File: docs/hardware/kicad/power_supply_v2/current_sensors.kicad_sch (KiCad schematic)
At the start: 5 parts, among them U11 INA180A3, U20 INA180A1, U21 INA180A1, U22 INA180A3, U23 INA180A3

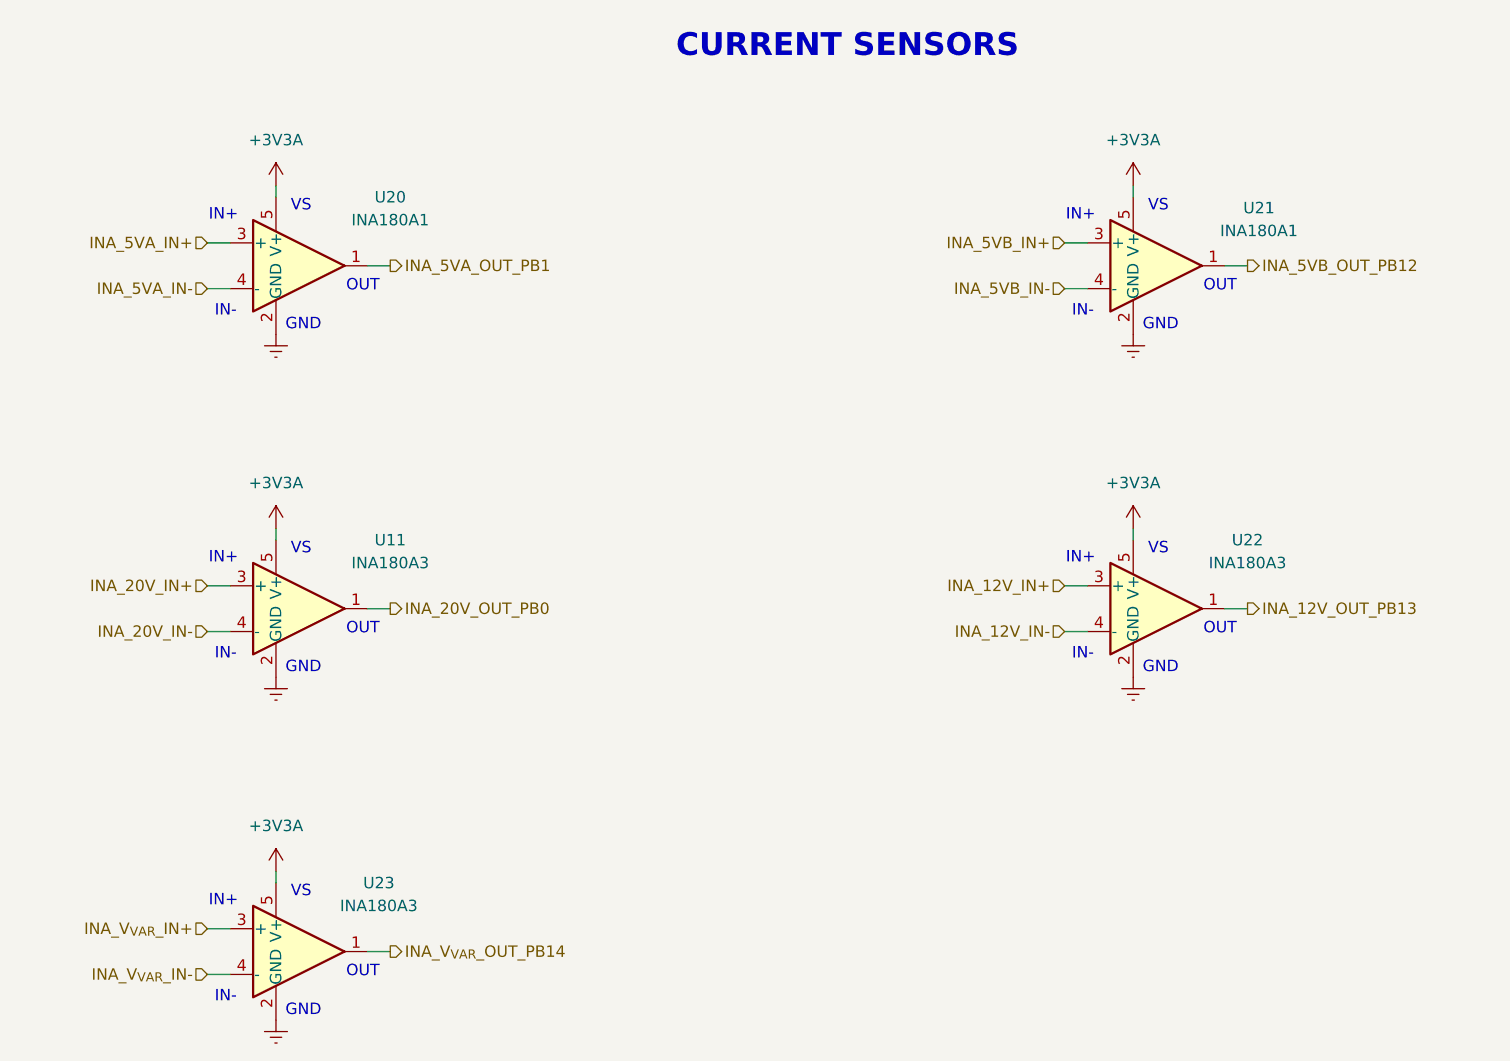
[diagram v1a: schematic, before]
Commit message: remove redundant switches for variable rail
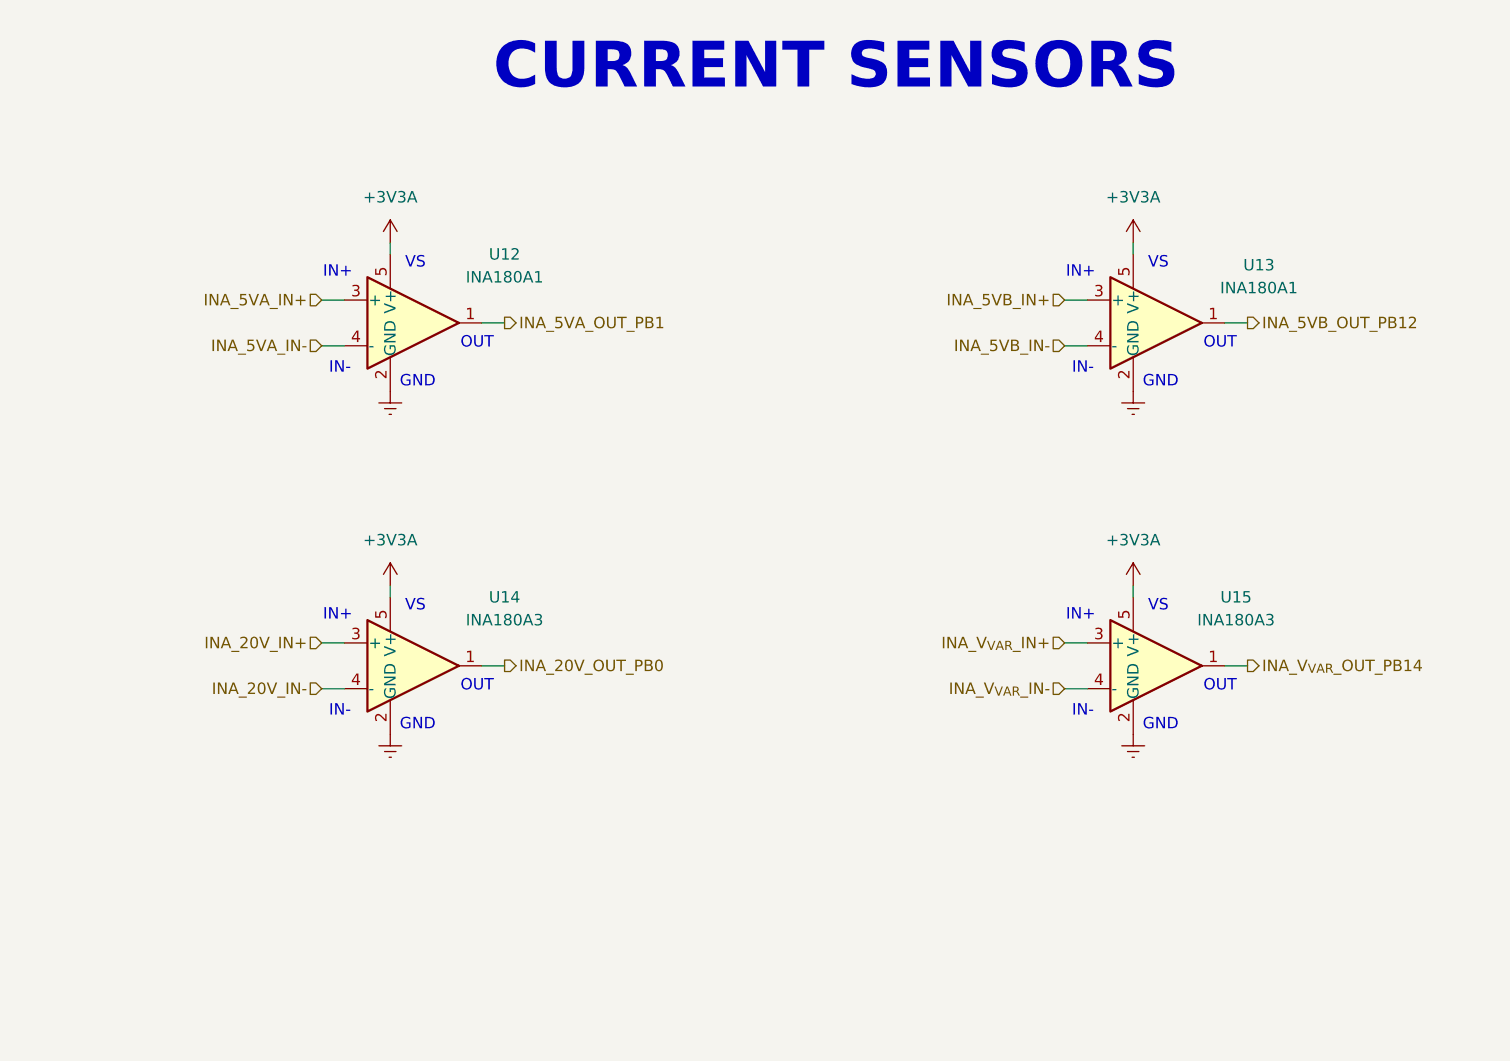
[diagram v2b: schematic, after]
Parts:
- removed U22: INA180A3, Package_TO_SOT_SMD:SOT-23-5, symbol Library:INA180A3
- renumbered U20 to U12, U21 to U13, U11 to U14, U23 to U15
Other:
- moved on the sheet: U12, U13, U14, U15

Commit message: update schematic to fix power rail node and update resistors to reflect series to reach target dividers
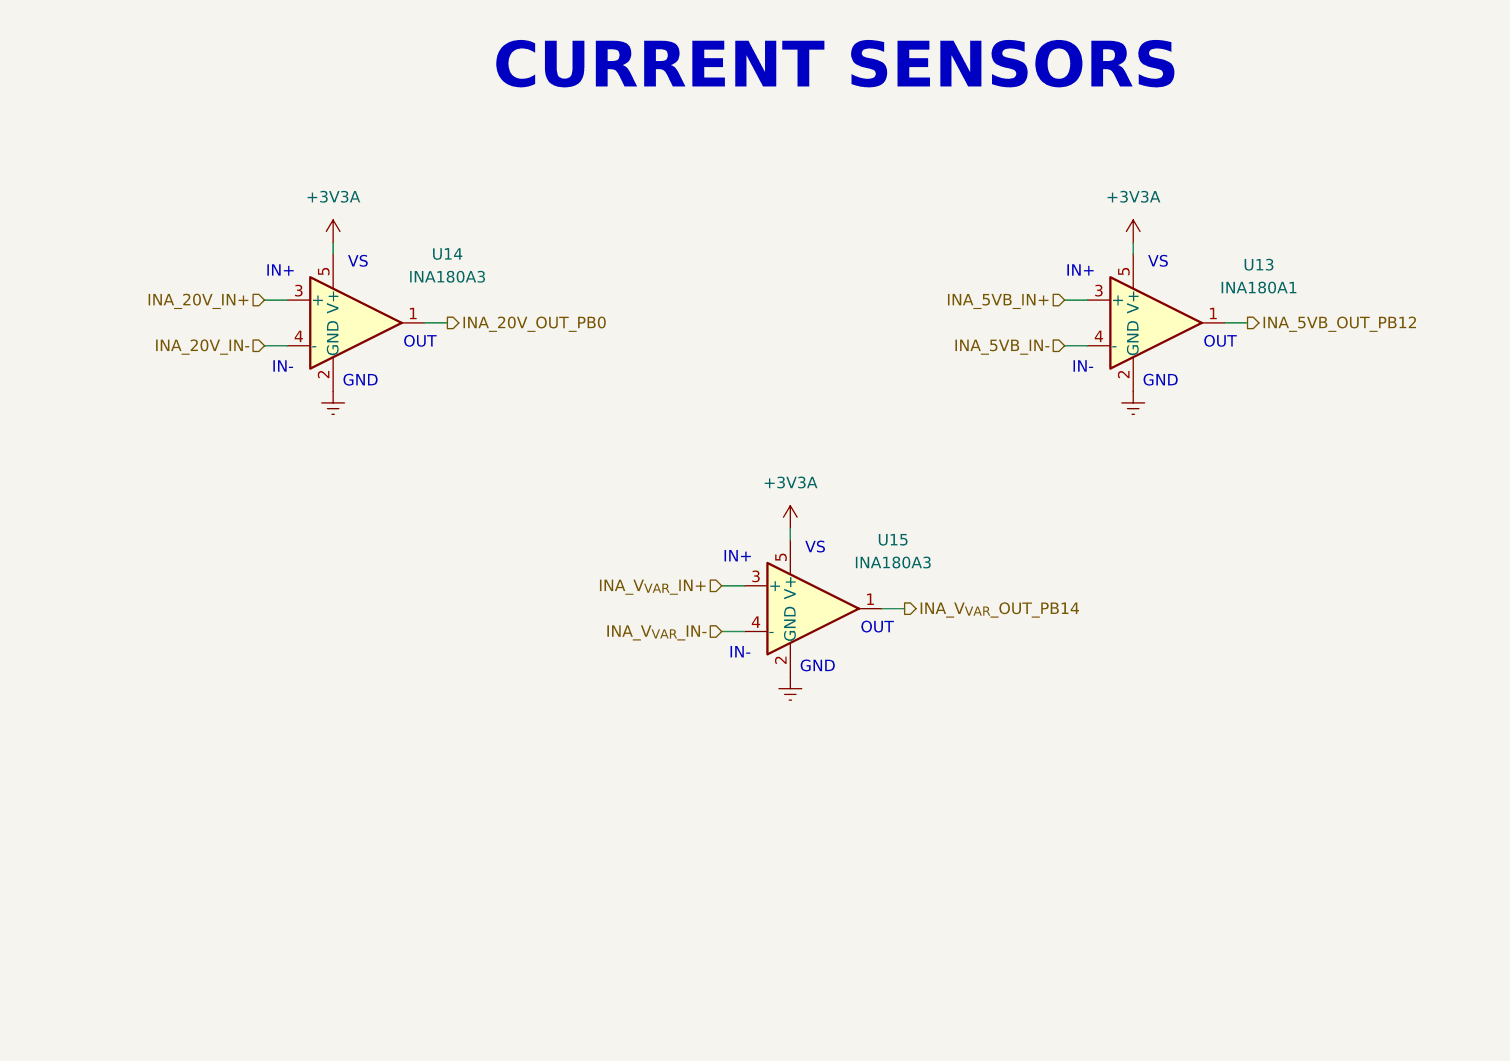
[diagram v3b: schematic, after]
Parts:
- removed U12: INA180A1, Package_TO_SOT_SMD:SOT-23-5, symbol Library:INA180A3
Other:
- moved on the sheet: U14, U15
